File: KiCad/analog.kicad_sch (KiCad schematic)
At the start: 6 parts, among them J1 Conn_01x02, U1 LM2596S-5

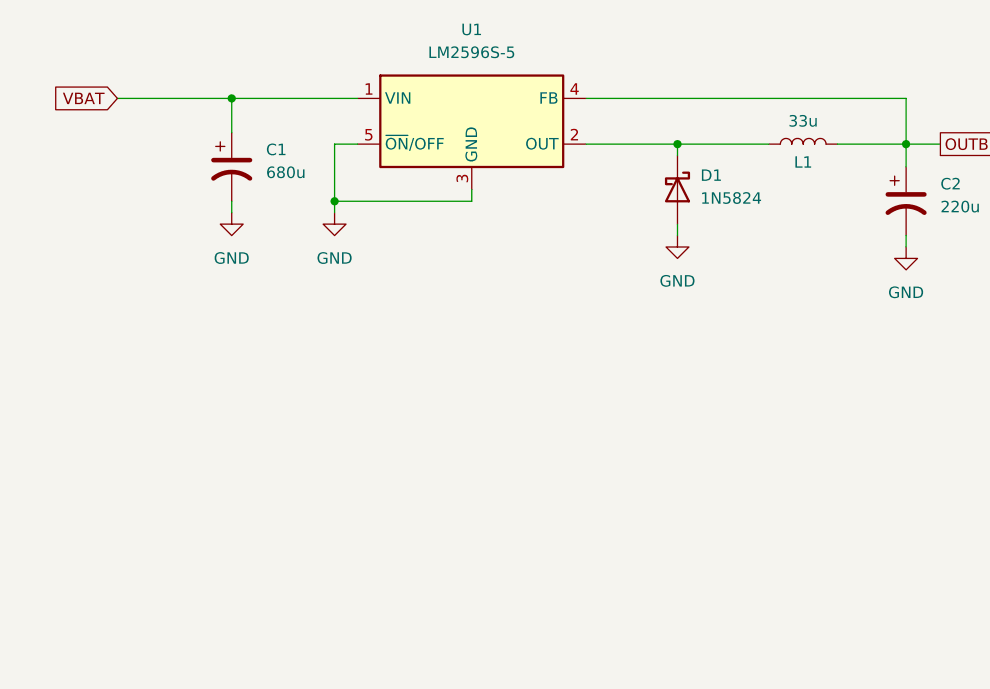
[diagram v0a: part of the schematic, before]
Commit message: Part de potencia acabada, concretar certs pins del micro
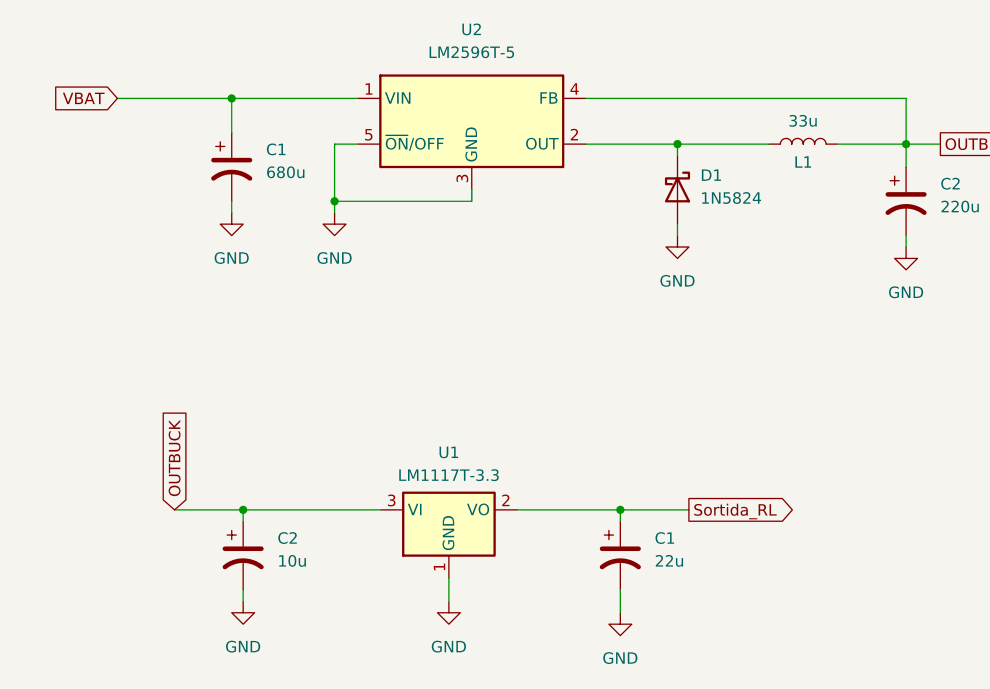
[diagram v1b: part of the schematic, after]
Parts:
- removed U1: LM2596S-5, Package_TO_SOT_SMD:TO-263-5_TabPin3, symbol Regulator_Switching:LM2596S-5
- added C1: 22u, symbol Device:C_Polarized_US
- added C2: 10u, symbol Device:C_Polarized_US
- added U1: LM1117T-3.3, Package_TO_SOT_THT:TO-220-3_Horizontal_TabDown, symbol Regulator_Linear:LM1117T-3.3
- added U2: LM2596T-5, Package_TO_SOT_THT:TO-220-5_P3.4x3.7mm_StaggerOdd_Lead3.8mm_Vertical, symbol Regulator_Switching:LM2596T-5
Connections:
- net GND: now also C1.2, C2.2, U1.1 (GND), U2.3 (GND), U2.5 (~{ON}/OFF)
- net OUTBUCK: now also C2.1, U1.3 (VI), U2.4 (FB)
- net VBAT: now also U2.1 (VIN)
- net at D1.1 (K), L1.1: now also U2.2 (OUT)
- new net Sortida_RL: C1.1, U1.2 (VO)

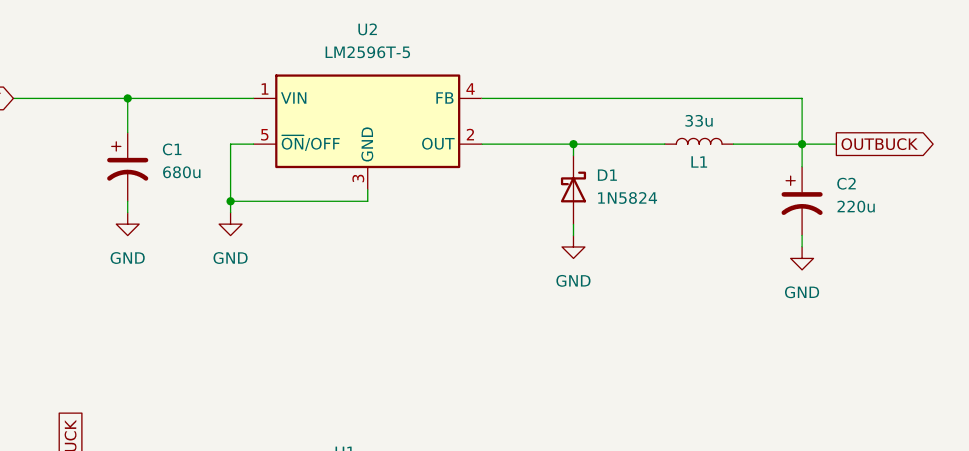
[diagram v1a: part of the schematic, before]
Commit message: Part de potencia acabada, concretar certs pins del micro
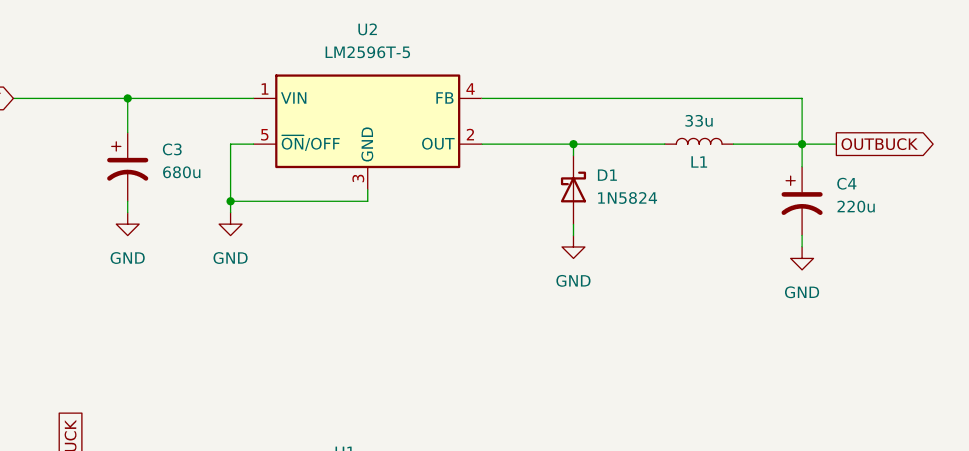
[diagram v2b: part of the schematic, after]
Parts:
- renumbered C1 to C3, C2 to C4
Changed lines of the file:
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@@
 		(dnp no)
 		(fields_autoplaced yes)
-		(property "Reference" "C1"
+		(property "Reference" "C3"
 			(at 78.74 55.2449 0)
 			(effects
@@
 				)
 			)
-			(project ""
-				(path "/c989196d-f442-462e-ad13-2ff17993bc1b/4c801c5d-4025-4c24-8da5-12ec47840bef"
-					(reference "C1")
+			(project "analog"
+				(path "/c989196d-f442-462e-ad13-2ff17993bc1b/9cc53e55-b115-43a5-9a22-06f8c68fe0c0"
+					(reference "C3")
 					(unit 1)
 				)
@@
 		(dnp no)
 		(fields_autoplaced yes)
-		(property "Reference" "#PWR04"
+		(property "Reference" "#PWR0102"
 			(at 149.86 72.39 0)
 			(effects
@@
 				)
 			)
-			(project "Combustible_projecte"
-				(path "/c989196d-f442-462e-ad13-2ff17993bc1b/4c801c5d-4025-4c24-8da5-12ec47840bef"
-					(reference "#PWR04")
+			(project "analog"
+				(path "/c989196d-f442-462e-ad13-2ff17993bc1b/9cc53e55-b115-43a5-9a22-06f8c68fe0c0"
+					(reference "#PWR0102")
 					(unit 1)
 				)
@@
 		(dnp no)
 		(fields_autoplaced yes)
-		(property "Reference" "C?"
+		(property "Reference" "C1"
 			(at 121.92 98.4249 0)
 			(effects
@@
 				)
 			)
-			(project "Combustible_projecte"
-				(path "/c989196d-f442-462e-ad13-2ff17993bc1b/4c801c5d-4025-4c24-8da5-12ec47840bef"
-					(reference "C?")
+			(project "analog"
+				(path "/c989196d-f442-462e-ad13-2ff17993bc1b/9cc53e55-b115-43a5-9a22-06f8c68fe0c0"
+					(reference "C1")
 					(unit 1)
 				)
@@
 		(dnp no)
 		(fields_autoplaced yes)
-		(property "Reference" "#PWR?"
+		(property "Reference" "#PWR01"
 			(at 99.06 111.76 0)
 			(effects
@@
 				)
 			)
-			(project "Combustible_projecte"
-				(path "/c989196d-f442-462e-ad13-2ff17993bc1b/4c801c5d-4025-4c24-8da5-12ec47840bef"
-					(reference "#PWR?")
+			(project "analog"
+				(path "/c989196d-f442-462e-ad13-2ff17993bc1b/9cc53e55-b115-43a5-9a22-06f8c68fe0c0"
+					(reference "#PWR01")
 					(unit 1)
 				)
@@
 		(dnp no)
 		(fields_autoplaced yes)
-		(property "Reference" "C?"
+		(property "Reference" "C2"
 			(at 80.01 98.4249 0)
 			(effects
@@
 				)
 			)
-			(project "Combustible_projecte"
-				(path "/c989196d-f442-462e-ad13-2ff17993bc1b/4c801c5d-4025-4c24-8da5-12ec47840bef"
-					(reference "C?")
+			(project "analog"
+				(path "/c989196d-f442-462e-ad13-2ff17993bc1b/9cc53e55-b115-43a5-9a22-06f8c68fe0c0"
+					(reference "C2")
 					(unit 1)
 				)
@@
 		(dnp no)
 		(fields_autoplaced yes)
-		(property "Reference" "#PWR03"
+		(property "Reference" "#PWR0101"
 			(at 124.46 71.12 0)
 			(effects
@@
 				)
 			)
-			(project "Combustible_projecte"
-				(path "/c989196d-f442-462e-ad13-2ff17993bc1b/4c801c5d-4025-4c24-8da5-12ec47840bef"
-					(reference "#PWR03")
+			(project "analog"
+				(path "/c989196d-f442-462e-ad13-2ff17993bc1b/9cc53e55-b115-43a5-9a22-06f8c68fe0c0"
+					(reference "#PWR0101")
 					(unit 1)
 				)
@@
 				)
 			)
-			(project ""
-				(path "/c989196d-f442-462e-ad13-2ff17993bc1b/4c801c5d-4025-4c24-8da5-12ec47840bef"
+			(project "analog"
+				(path "/c989196d-f442-462e-ad13-2ff17993bc1b/9cc53e55-b115-43a5-9a22-06f8c68fe0c0"
 					(reference "D1")
 					(unit 1)
@@
 		(dnp no)
 		(fields_autoplaced yes)
-		(property "Reference" "U?"
+		(property "Reference" "U2"
 			(at 101.6 41.91 0)
 			(effects
@@
 				)
 			)
-			(project "Combustible_projecte"
-				(path "/c989196d-f442-462e-ad13-2ff17993bc1b/4c801c5d-4025-4c24-8da5-12ec47840bef"
-					(reference "U?")
+			(project ""
+				(path "/c989196d-f442-462e-ad13-2ff17993bc1b/9cc53e55-b115-43a5-9a22-06f8c68fe0c0"
+					(reference "U2")
 					(unit 1)
 				)
@@
 		(dnp no)
 		(fields_autoplaced yes)
-		(property "Reference" "#PWR05"
+		(property "Reference" "#PWR0103"
 			(at 74.93 68.58 0)
 			(effects
@@
 				)
 			)
-			(project "Combustible_projecte"
-				(path "/c989196d-f442-462e-ad13-2ff17993bc1b/4c801c5d-4025-4c24-8da5-12ec47840bef"
-					(reference "#PWR05")
+			(project "analog"
+				(path "/c989196d-f442-462e-ad13-2ff17993bc1b/9cc53e55-b115-43a5-9a22-06f8c68fe0c0"
+					(reference "#PWR0103")
 					(unit 1)
 				)
@@
 		(dnp no)
 		(fields_autoplaced yes)
-		(property "Reference" "#PWR02"
+		(property "Reference" "#PWR0104"
 			(at 86.36 68.58 0)
 			(effects
@@
 				)
 			)
-			(project ""
-				(path "/c989196d-f442-462e-ad13-2ff17993bc1b/4c801c5d-4025-4c24-8da5-12ec47840bef"
-					(reference "#PWR02")
+			(project "analog"
+				(path "/c989196d-f442-462e-ad13-2ff17993bc1b/9cc53e55-b115-43a5-9a22-06f8c68fe0c0"
+					(reference "#PWR0104")
 					(unit 1)
 				)
@@
 		(dnp no)
 		(fields_autoplaced yes)
-		(property "Reference" "C2"
+		(property "Reference" "C4"
 			(at 153.67 59.0549 0)
 			(effects
@@
 				)
 			)
-			(project "Combustible_projecte"
-				(path "/c989196d-f442-462e-ad13-2ff17993bc1b/4c801c5d-4025-4c24-8da5-12ec47840bef"
-					(reference "C2")
+			(project "analog"
+				(path "/c989196d-f442-462e-ad13-2ff17993bc1b/9cc53e55-b115-43a5-9a22-06f8c68fe0c0"
+					(reference "C4")
 					(unit 1)
 				)
@@
 		(dnp no)
 		(fields_autoplaced yes)
-		(property "Reference" "#PWR?"
+		(property "Reference" "#PWR02"
 			(at 76.2 111.76 0)
 			(effects
@@
 				)
 			)
-			(project "Combustible_projecte"
-				(path "/c989196d-f442-462e-ad13-2ff17993bc1b/4c801c5d-4025-4c24-8da5-12ec47840bef"
-					(reference "#PWR?")
+			(project "analog"
+				(path "/c989196d-f442-462e-ad13-2ff17993bc1b/9cc53e55-b115-43a5-9a22-06f8c68fe0c0"
+					(reference "#PWR02")
 					(unit 1)
 				)
@@
 		(dnp no)
 		(fields_autoplaced yes)
-		(property "Reference" "U?"
+		(property "Reference" "U1"
 			(at 99.06 88.9 0)
 			(effects
@@
 				)
 			)
-			(project "Combustible_projecte"
-				(path "/c989196d-f442-462e-ad13-2ff17993bc1b/4c801c5d-4025-4c24-8da5-12ec47840bef"
-					(reference "U?")
+			(project ""
+				(path "/c989196d-f442-462e-ad13-2ff17993bc1b/9cc53e55-b115-43a5-9a22-06f8c68fe0c0"
+					(reference "U1")
 					(unit 1)
 				)
@@
 		(dnp no)
 		(fields_autoplaced yes)
-		(property "Reference" "#PWR?"
+		(property "Reference" "#PWR03"
 			(at 118.11 113.03 0)
 			(effects
@@
 				)
 			)
-			(project "Combustible_projecte"
-				(path "/c989196d-f442-462e-ad13-2ff17993bc1b/4c801c5d-4025-4c24-8da5-12ec47840bef"
-					(reference "#PWR?")
+			(project "analog"
+				(path "/c989196d-f442-462e-ad13-2ff17993bc1b/9cc53e55-b115-43a5-9a22-06f8c68fe0c0"
+					(reference "#PWR03")
 					(unit 1)
 				)
@@
 				)
 			)
-			(project ""
-				(path "/c989196d-f442-462e-ad13-2ff17993bc1b/4c801c5d-4025-4c24-8da5-12ec47840bef"
+			(project "analog"
+				(path "/c989196d-f442-462e-ad13-2ff17993bc1b/9cc53e55-b115-43a5-9a22-06f8c68fe0c0"
 					(reference "J1")
 					(unit 1)
@@
 		(dnp no)
 		(fields_autoplaced yes)
-		(property "Reference" "#PWR01"
+		(property "Reference" "#PWR0105"
 			(at 31.75 63.5 0)
 			(effects
@@
 				)
 			)
-			(project ""
-				(path "/c989196d-f442-462e-ad13-2ff17993bc1b/4c801c5d-4025-4c24-8da5-12ec47840bef"
-					(reference "#PWR01")
+			(project "analog"
+				(path "/c989196d-f442-462e-ad13-2ff17993bc1b/9cc53e55-b115-43a5-9a22-06f8c68fe0c0"
+					(reference "#PWR0105")
 					(unit 1)
 				)
@@
 				)
 			)
-			(project ""
-				(path "/c989196d-f442-462e-ad13-2ff17993bc1b/4c801c5d-4025-4c24-8da5-12ec47840bef"
+			(project "analog"
+				(path "/c989196d-f442-462e-ad13-2ff17993bc1b/9cc53e55-b115-43a5-9a22-06f8c68fe0c0"
 					(reference "L1")
 					(unit 1)
@@
 		)
 	)
-	(sheet_instances
-		(path "/"
-			(page "1")
-		)
-	)
-	(embedded_fonts no)
 )

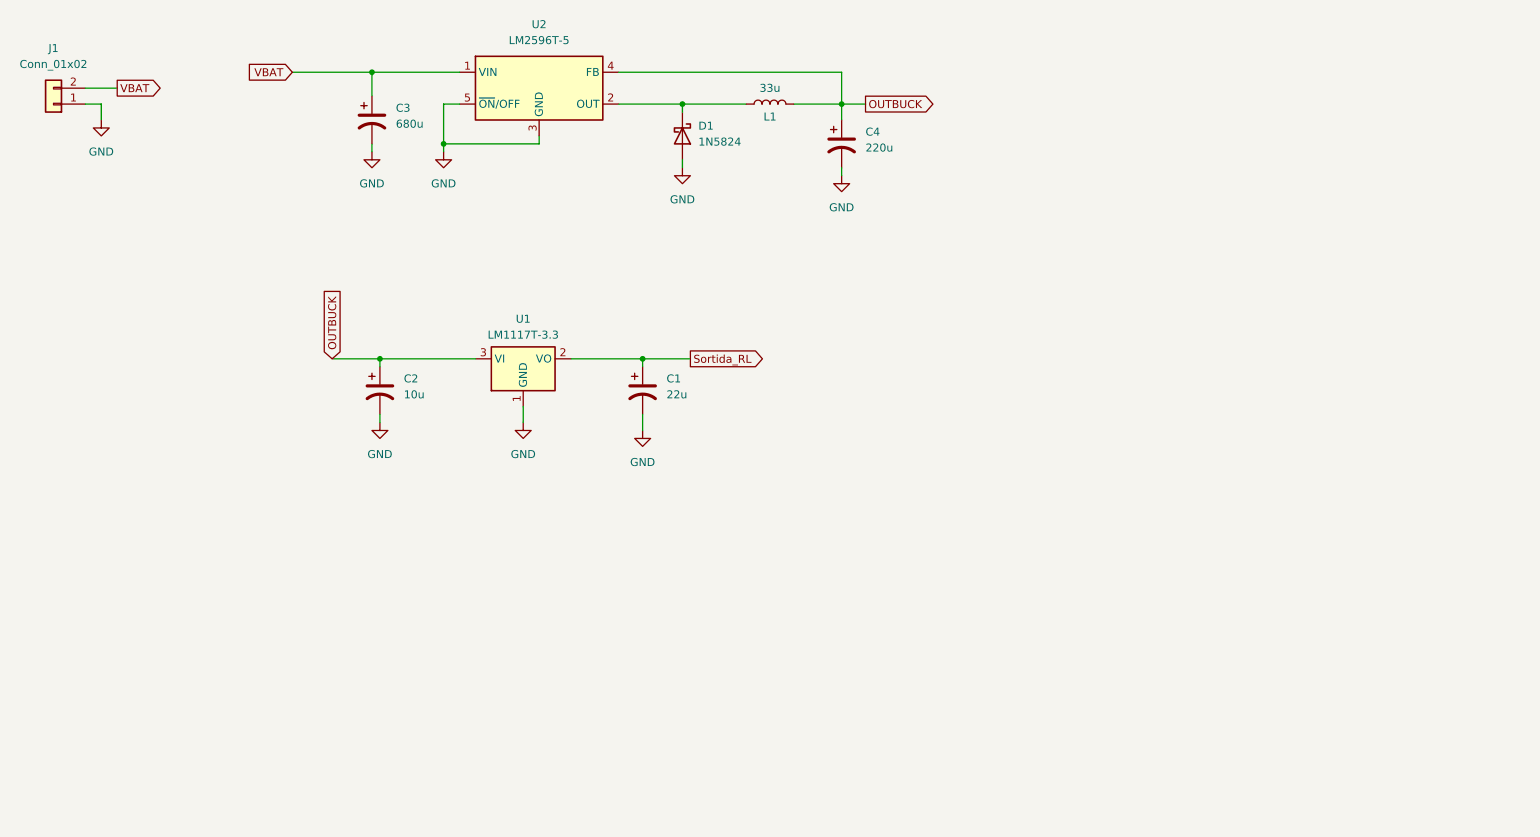
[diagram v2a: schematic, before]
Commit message: Part de potencia moguda al sheet de analogica, esborrat el sheet de potencia
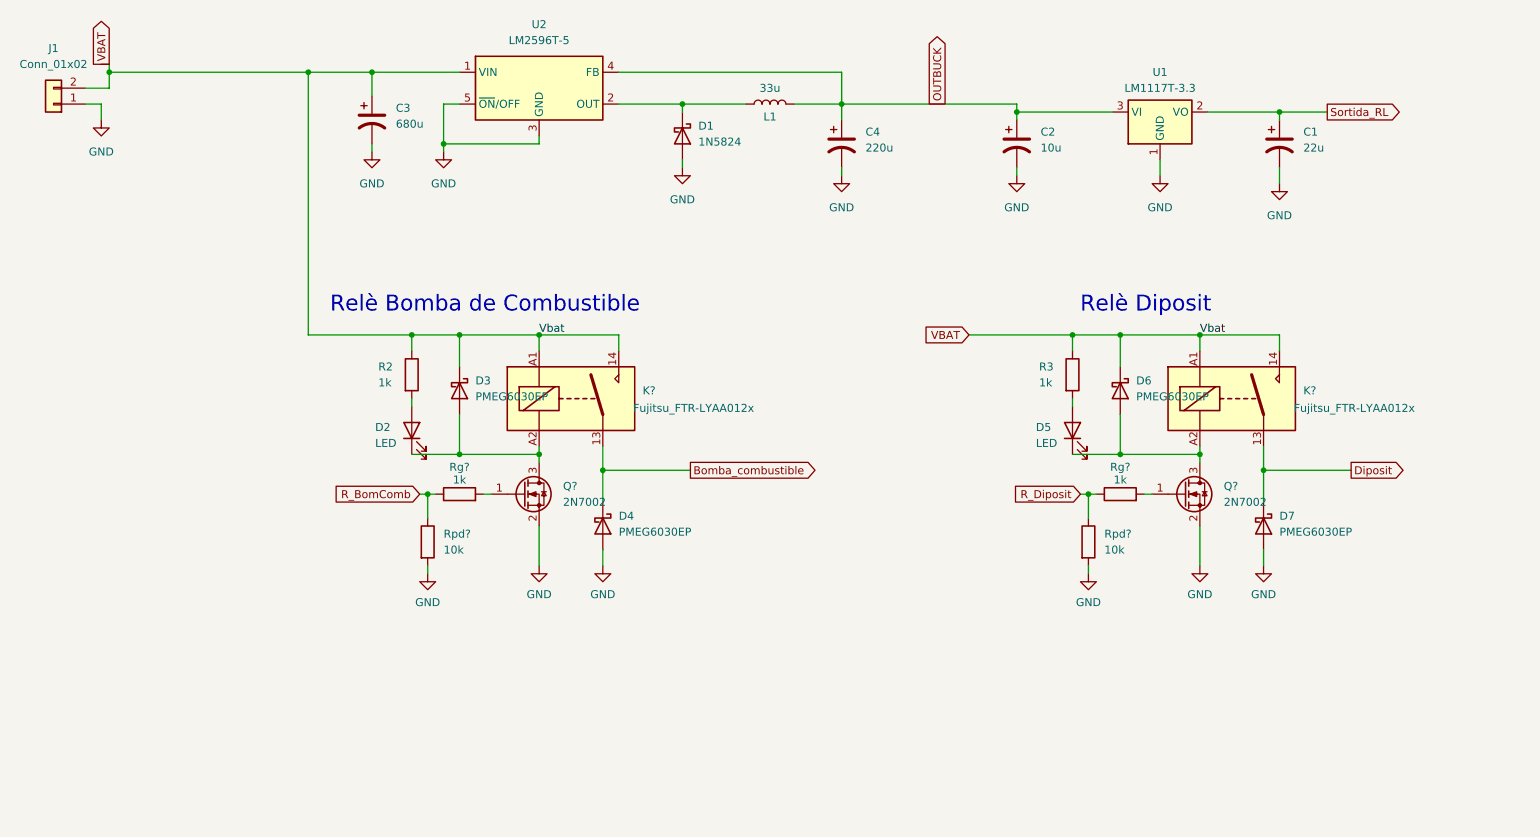
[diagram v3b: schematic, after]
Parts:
- added D2, D5: LED, LED_SMD:LED_0805_2012Metric, symbol Device:LED
- added D3, D4, D6, D7: PMEG6030EP, Diode_SMD:D_SOD-128, symbol Diode:PMEG6030EP
- added K? (x2): Fujitsu_FTR-LYAA012x, Relay_THT:Relay_SPST-NO_Fujitsu_FTR-LYAA005x_FormA_Vertical, symbol Relay:Fujitsu_FTR-LYAA005x
- added Q? (x2): 2N7002, Package_TO_SOT_SMD:SOT-23, symbol Transistor_FET:2N7002
- added R2, R3, Rg? (x2): 1k, Resistor_SMD:R_1206_3216Metric, symbol Device:R
- added Rpd? (x2): 10k, Resistor_SMD:R_1206_3216Metric, symbol Device:R
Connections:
- net GND: now also D4.2 (A), D7.2 (A), Q?.2 (S), Q?.2 (S), Rpd?.2, Rpd?.2
- net VBAT: now also D3.1 (K), D6.1 (K), K?.14, K?.14, K?.A1, K?.A1, R2.1, R3.1
- new net: D2.1 (K), D3.2 (A), K?.A2, Q?.3 (D)
- new net: Q?.1 (G), Rg?.2 (x2)
- new net: D2.2 (A), R2.2
- new net: D5.1 (K), D6.2 (A), K?.A2, Q?.3 (D)
- new net: D5.2 (A), R3.2
- new net Bomba_combustible: D4.1 (K), K?.13
- new net Diposit: D7.1 (K), K?.13
- new net R_BomComb: Rg?.1, Rpd?.1
- new net R_Diposit: Rg?.1, Rpd?.1
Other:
- note added: "Relè Bomba de Combustible"
- note added: "Relè Diposit"
- moved on the sheet: C1, C2, U1

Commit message: Errores ERC corregidos, instanciaciones arregladas
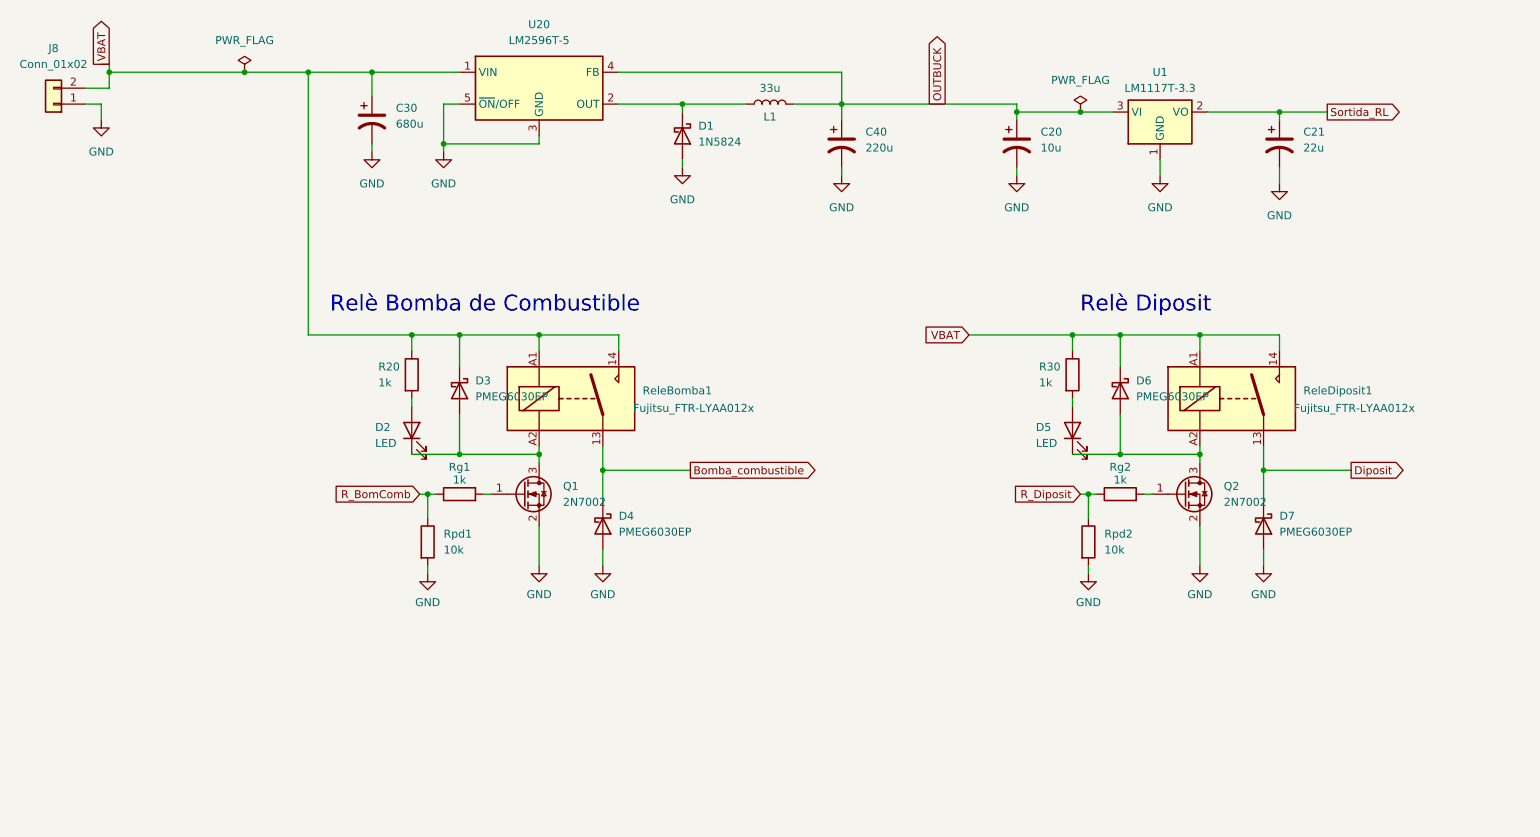
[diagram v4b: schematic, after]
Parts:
- gave numbers to parts that had none: 8
- renumbered C2 to C20, C1 to C21, C3 to C30, C4 to C40, J1 to J8, R2 to R20, R3 to R30, U2 to U20

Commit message: canvi d'etiquetes
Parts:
- renumbered C21 to C1, C20 to C2, C30 to C3, C40 to C4, D3 to D?, D5 to D?, D2 to D?, D7 to D?, D4 to D?, D6 to D?, J8 to J1, Q2 to Q?, Q1 to Q?, R20 to R?, R30 to R?, ReleBomba1 to ReleBomba?, ReleDiposit1 to ReleDiposit?, Rg2 to Rg?, Rg1 to Rg?, Rpd2 to Rpd?, Rpd1 to Rpd?, U20 to U2
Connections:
- net OUTBUCK renamed 5v
- net Sortida_RL renamed 3v3
